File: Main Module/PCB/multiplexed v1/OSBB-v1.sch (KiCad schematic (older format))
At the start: 26 parts, among them P1 AUX 1-3, P14 EXTRA Pins, P2 Wire to Teensy VUSB, P3 +3.3V, P4 Pit Limiter, P5 Rotary Encoders, P6 BTN 1-32, Q1 NPN, Q2 NPN, Q3 NPN, Q4 NPN, U1 74HC4051, U2 74HC4051, U3 74HC4051, U4 74HC4051, U5 Teensy3.2

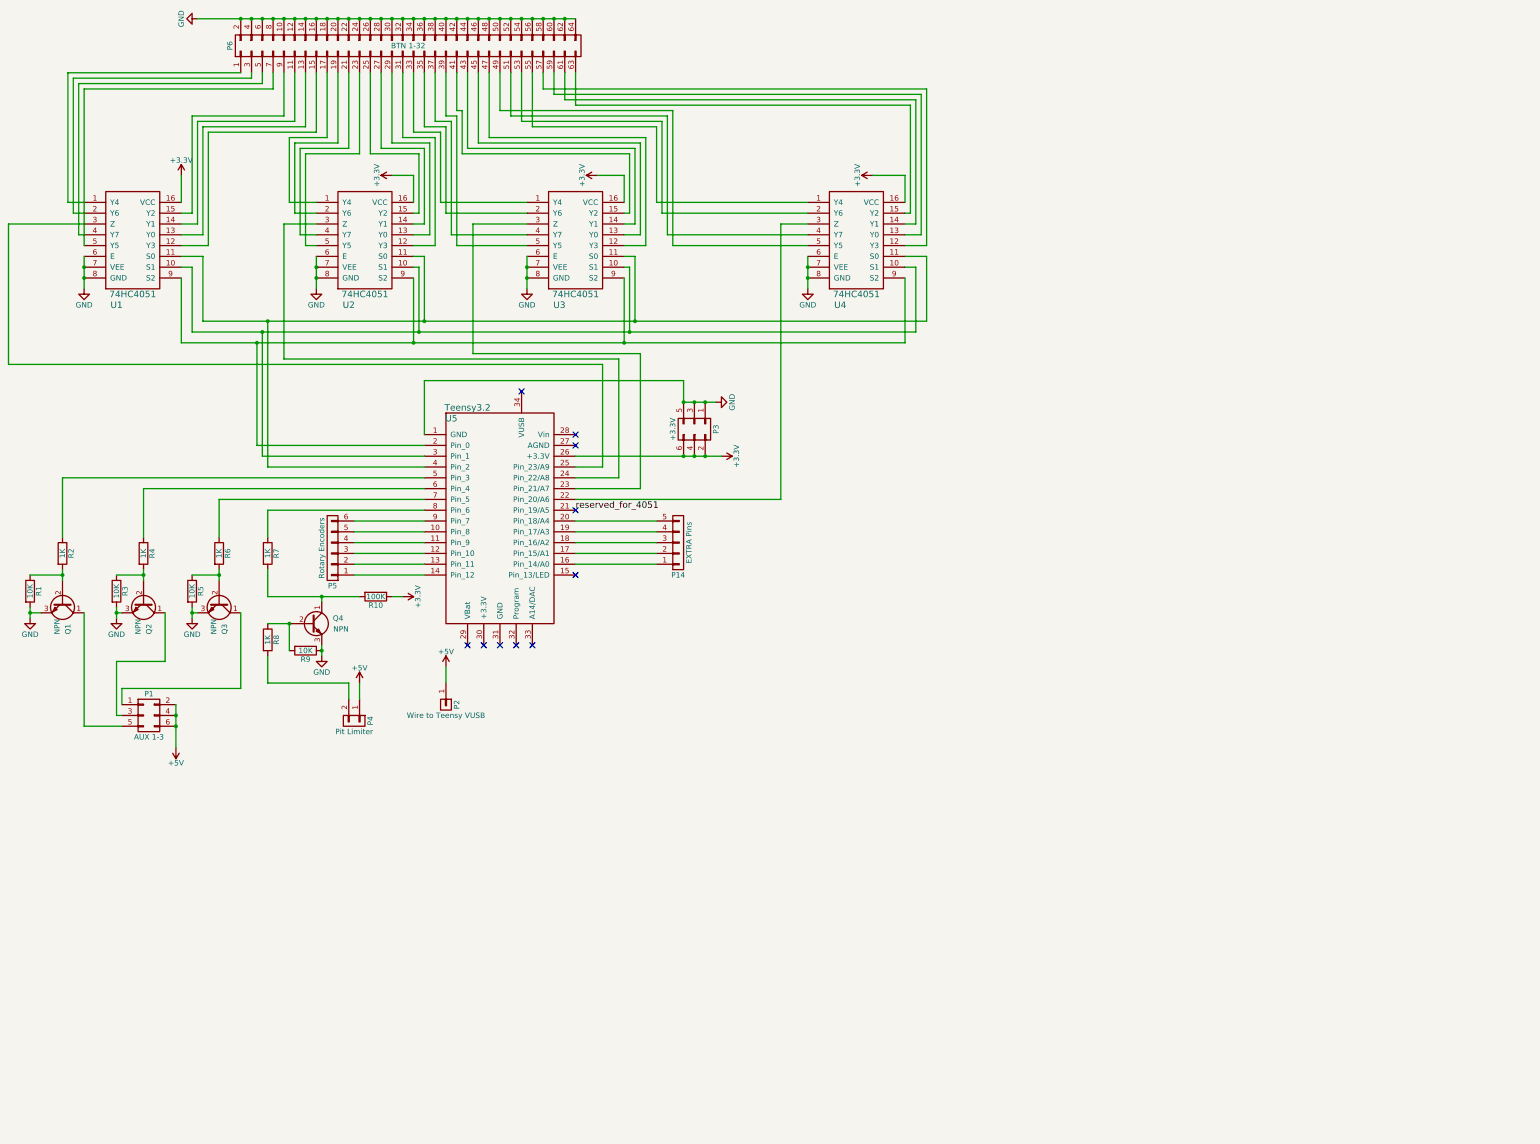
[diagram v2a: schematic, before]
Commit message: * PCB RC5-DEV adjusting button schematic to pull input low * now with M3 mounting hols * fixed missing silkscreen
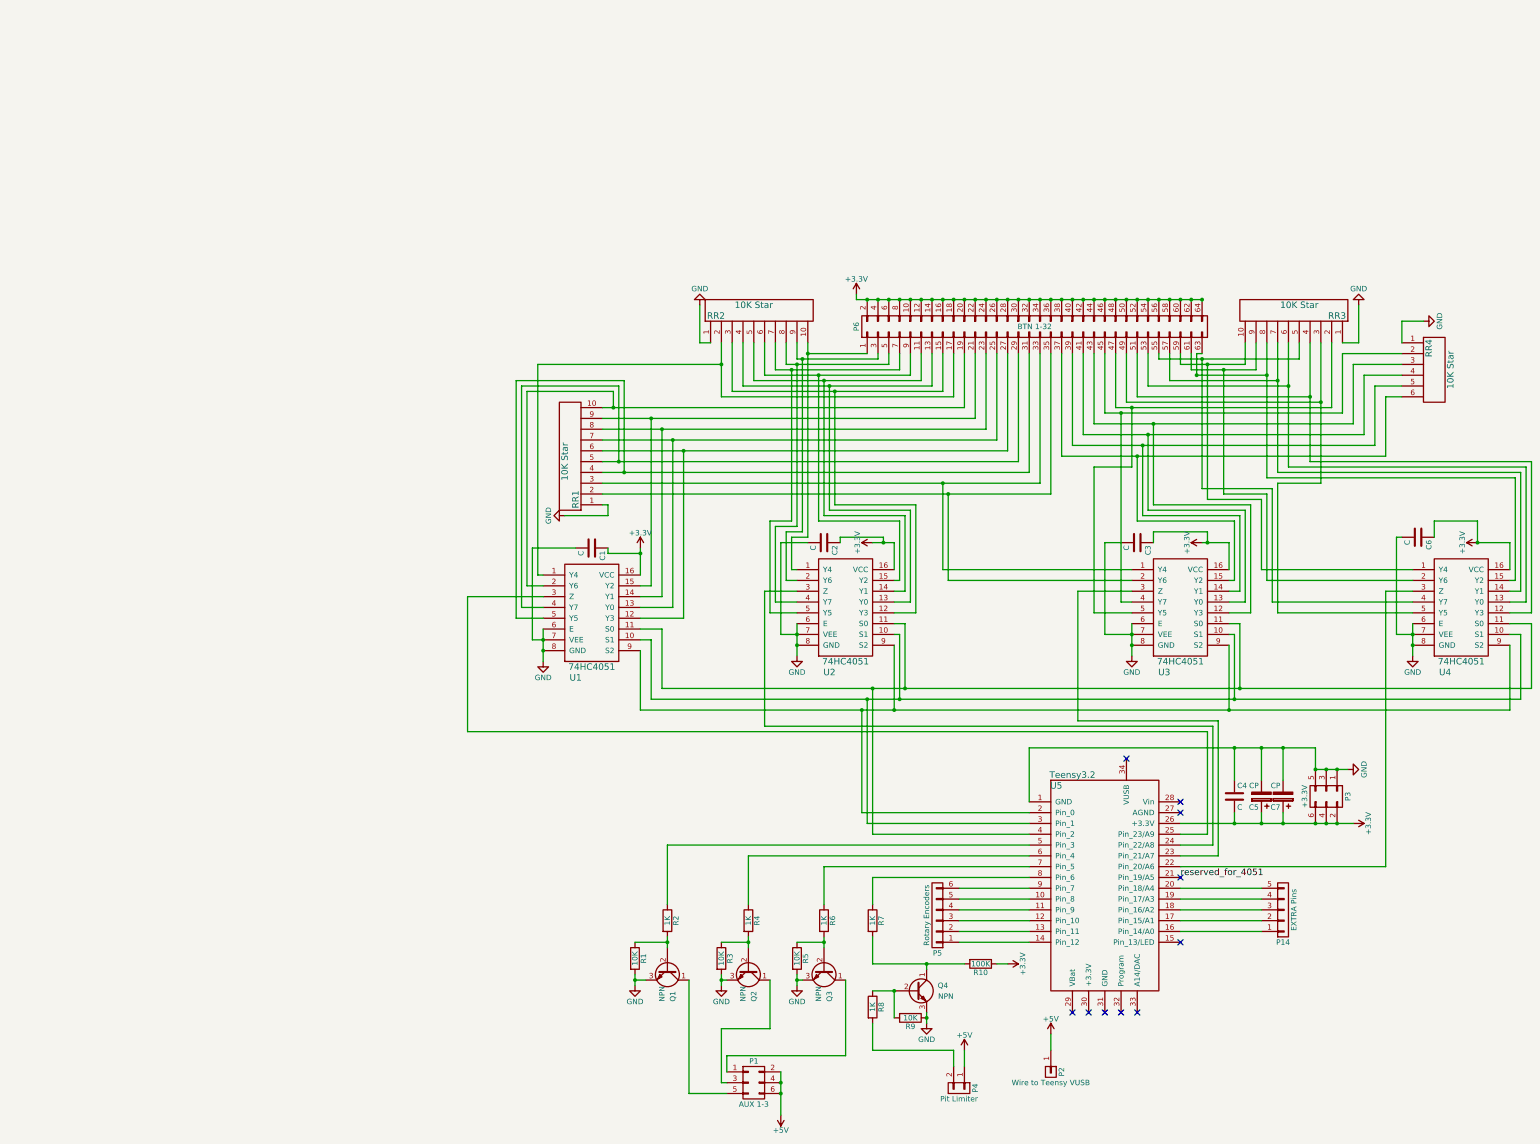
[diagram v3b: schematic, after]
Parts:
- added C1, C2, C3, C4, C6: C, Capacitors_ThroughHole:C_Disc_D3_P2.5, symbol C
- added C5, C7: CP, Capacitors_ThroughHole:C_Radial_D5_L11_P2, symbol CP
- added RR1, RR2, RR3: 10K Star, Pin_Headers:Pin_Header_Straight_1x10, symbol RESISTOR-STAR10
- added RR4: 10K Star, Pin_Headers:Pin_Header_Straight_1x06, symbol RESISTOR-STAR6
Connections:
- net +3V3: now also P6.10 (P10), P6.12 (P12), P6.14 (P14), P6.16 (P16), P6.18 (P18), P6.2 (P2), P6.20 (P20), P6.22 (P22), P6.24 (P24), P6.26 (P26), P6.28 (P28), P6.30 (P30), P6.32 (P32), P6.34 (P34), P6.36 (P36), P6.38 (P38), P6.4 (P4), P6.40 (P40), P6.42 (P42), P6.44 (P44), P6.46 (P46), P6.48 (P48), P6.50 (P50), P6.52 (P52), P6.54 (P54), P6.56 (P56), P6.58 (P58), P6.6 (P6), P6.60 (P60), P6.62 (P62), P6.64 (P64), P6.8 (P8), C1.1, C2.1, C3.1, C4.2, C5.1, C6.1, C7.1
- net GND: now also C1.2, C2.2, C3.2, C4.1, C5.2, C6.2, C7.2, RR1.1, RR2.1, RR3.1, RR4.1; no longer P6.10 (P10), P6.12 (P12), P6.14 (P14), P6.16 (P16), P6.18 (P18), P6.2 (P2), P6.20 (P20), P6.22 (P22), P6.24 (P24), P6.26 (P26), P6.28 (P28), P6.30 (P30), P6.32 (P32), P6.34 (P34), P6.36 (P36), P6.38 (P38), P6.4 (P4), P6.40 (P40), P6.42 (P42), P6.44 (P44), P6.46 (P46), P6.48 (P48), P6.50 (P50), P6.52 (P52), P6.54 (P54), P6.56 (P56), P6.58 (P58), P6.6 (P6), P6.60 (P60), P6.62 (P62), P6.64 (P64), P6.8 (P8)
- net at U2.1 (Y4): now also P6.1 (P1), RR2.10; no longer P6.17 (P17)
- net at U2.12 (Y3): now also P6.15 (P15), RR2.3; no longer P6.31 (P31)
- net at U2.13 (Y0): now also P6.13 (P13), RR2.4; no longer P6.29 (P29)
- net at U2.14 (Y1): now also P6.11 (P11), RR2.5; no longer P6.27 (P27)
- net at U2.15 (Y2): now also P6.9 (P9), RR2.6; no longer P6.25 (P25)
- net at U2.2 (Y6): now also P6.3 (P3), RR2.9; no longer P6.19 (P19)
- net at U2.4 (Y7): now also P6.5 (P5), RR2.8; no longer P6.21 (P21)
- net at U2.5 (Y5): now also P6.7 (P7), RR2.7; no longer P6.23 (P23)
- net at P6.33 (P33), U3.1 (Y4): now also RR1.3
- net at U3.12 (Y3): now also P6.43 (P43), RR4.3; no longer P6.47 (P47)
- net at U3.13 (Y0): now also P6.41 (P41), RR4.4; no longer P6.45 (P45)
- net at U3.14 (Y1): now also P6.39 (P39), RR4.5; no longer P6.43 (P43)
- net at U3.15 (Y2): now also P6.37 (P37), RR4.6; no longer P6.41 (P41)
- net at P6.35 (P35), U3.2 (Y6): now also RR1.2
- net at U3.4 (Y7): now also P6.45 (P45), RR4.2; no longer P6.37 (P37)
- net at U3.5 (Y5): now also P6.47 (P47), RR3.2; no longer P6.39 (P39)
- net at U1.1 (Y4): now also P6.17 (P17), RR2.2; no longer P6.1 (P1)
- net at U1.12 (Y3): now also P6.27 (P27), RR1.6; no longer P6.15 (P15)
- net at U1.13 (Y0): now also P6.25 (P25), RR1.7; no longer P6.13 (P13)
- net at U1.14 (Y1): now also P6.23 (P23), RR1.8; no longer P6.11 (P11)
- net at U1.15 (Y2): now also P6.21 (P21), RR1.9; no longer P6.9 (P9)
- net at U1.2 (Y6): now also P6.19 (P19), RR1.10; no longer P6.3 (P3)
- net at U1.4 (Y7): now also P6.29 (P29), RR1.5; no longer P6.5 (P5)
- net at U1.5 (Y5): now also P6.31 (P31), RR1.4; no longer P6.7 (P7)
- net at U4.1 (Y4): now also P6.59 (P59), RR3.10; no longer P6.55 (P55)
- net at U4.12 (Y3): now also P6.51 (P51), RR3.4; no longer P6.57 (P57)
- net at U4.13 (Y0): now also P6.53 (P53), RR3.6; no longer P6.59 (P59)
- net at U4.14 (Y1): now also P6.57 (P57), RR3.7; no longer P6.61 (P61)
- net at P6.63 (P63), U4.15 (Y2): now also RR3.8
- net at U4.2 (Y6): now also P6.61 (P61), RR3.9; no longer P6.53 (P53)
- net at U4.4 (Y7): now also P6.55 (P55), RR3.5; no longer P6.51 (P51)
- net at P6.49 (P49), U4.5 (Y5): now also RR3.3
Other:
- moved on the sheet: P1, P14, P2, P3, P4, P5, P6, Q1, Q2, Q3, Q4, R1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

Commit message: * updated schematic with PTC fuse
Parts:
- removed C1, C2, C3, C6: C, Capacitors_ThroughHole:C_Disc_D3_P2.5, symbol C
- added PTC1, PTC2: h0.3A/t0.5A, MOBB-KiCad-Lib:PTC-5MM, symbol F_Small
- added R11: 10K, Resistors_ThroughHole:Resistor_Horizontal_RM7mm, symbol R
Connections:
- wire segments 355 -> 440

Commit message: * current work of PCB RC6 - WIP * added PTC fuses for 3.3V and 5V to protect the PC in case of accidental short circuit * added 2x1 straight pin header which connects to pin13. this may late be used for feedback. not used yet * added solder pads for optional SMD 0805 capacitors * position of mounting holes has moved again. now final and written on PCB back side * distance between pit, AUX, encoder, .... pin headers now multiples of 2.54mm
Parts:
- removed C5: CP, Capacitors_ThroughHole:C_Radial_D5_L11_P2, symbol CP
- removed R11, R3, R5, R9: 10K, Resistors_ThroughHole:Resistor_Horizontal_RM7mm, symbol R
- removed R2, R4, R6, R7, R8: 1K, Resistors_ThroughHole:Resistor_Horizontal_RM7mm, symbol R
- added C1: C, Capacitors_SMD:C_0805_HandSoldering, symbol C
- added P7: LED, Pin_Headers:Pin_Header_Straight_1x02, symbol CONN_01X02
- added RR5: 10K-STAR10, Pin_Headers:Pin_Header_Straight_1x10, symbol RESISTOR-STAR10
- added RR6: 1K-STAR10, Pin_Headers:Pin_Header_Straight_1x10, symbol RESISTOR-STAR10
- C4: footprint Capacitors_ThroughHole:C_Disc_D3_P2.5 -> Capacitors_SMD:C_0805_HandSoldering
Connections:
- net labels added: PINHEADERSRC
- wire segments 440 -> 372
- no-connect marks 10 -> 9
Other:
- moved on the sheet: C4, P3
